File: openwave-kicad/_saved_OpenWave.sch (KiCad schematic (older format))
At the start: 38 parts, among them IC1 STM32F405RGT, J1 USB_OTG, J2 503182-1852, SW1 SW_Push, Y1 8MHz, Y2 32.768KHz

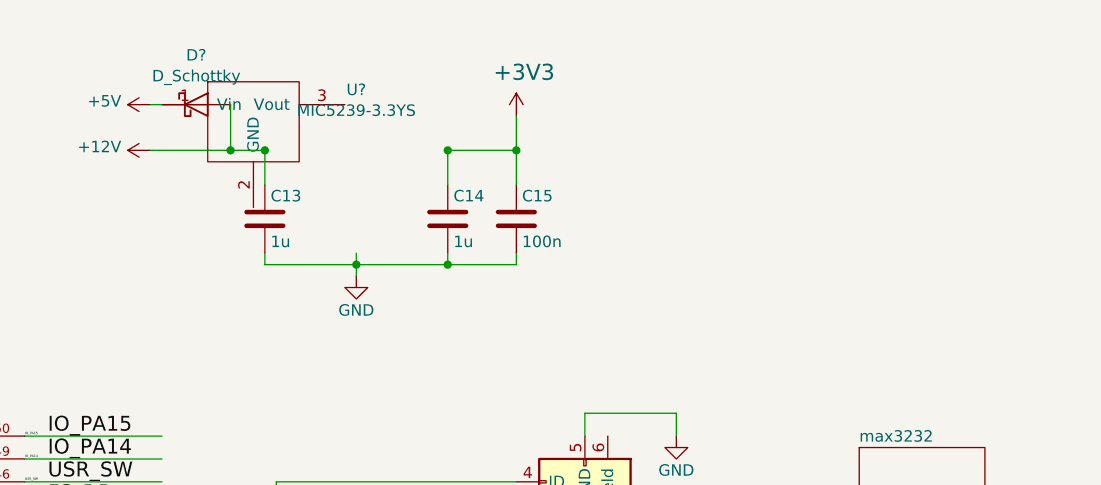
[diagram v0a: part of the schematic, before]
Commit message: added bluetooth header, 4.2v reg
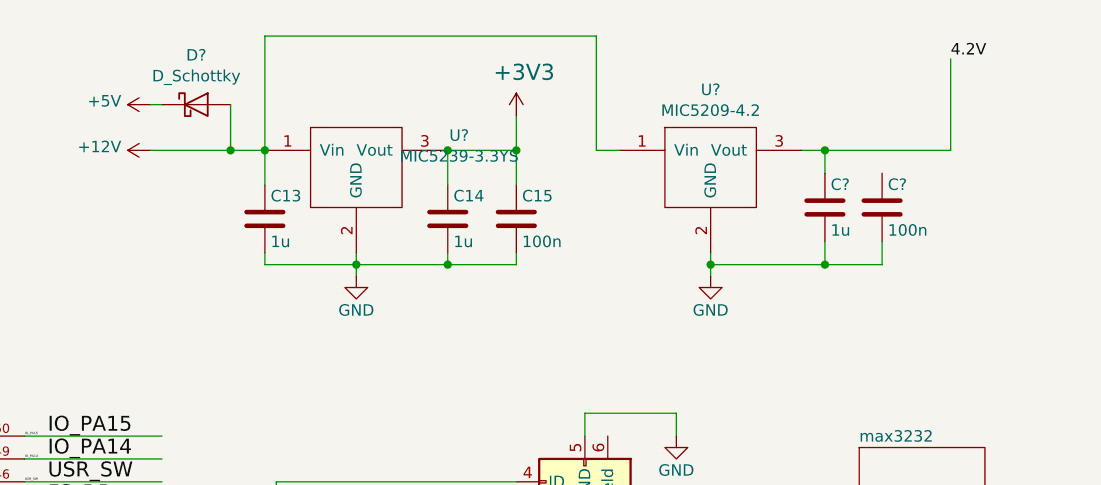
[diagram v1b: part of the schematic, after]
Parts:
- added C?: 1u, Capacitors_SMD:C_0603, symbol Device:C
- added C?: 100n, Capacitors_SMD:C_0603, symbol Device:C
- added U?: MIC5209-4.2, symbol wattnotions:MIC5209-4.2
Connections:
- net labels added: 4.2V
- wire segments 188 -> 202
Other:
- moved on the sheet: U?
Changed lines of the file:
@@
 L wattnotions:MIC5239-3.3YS U?
 U 1 1 5CAAC9EC
-P 8150 1000
-F 0 "U?" H 8150 1165 50  0000 C CNN
-F 1 "MIC5239-3.3YS" H 8150 1074 50  0000 C CNN
-F 2 "" H 8150 950 50  0001 C CNN
-F 3 "" H 8150 950 50  0001 C CNN
-	1    8150 1000
+P 8600 1200
+F 0 "U?" H 8600 1365 50  0000 C CNN
+F 1 "MIC5239-3.3YS" H 8600 1274 50  0000 C CNN
+F 2 "" H 8600 1150 50  0001 C CNN
+F 3 "" H 8600 1150 50  0001 C CNN
+	1    8600 1200
 	1    0    0    -1
 $EndComp
@@
 Wire Wire Line
 	7250 1100 7600 1100
+$Comp
+L wattnotions:MIC5209-4.2 U?
+U 1 1 5CB69853
+P 9700 1150
+F 0 "U?" H 9700 1465 50  0000 C CNN
+F 1 "MIC5209-4.2" H 9700 1374 50  0000 C CNN
+F 2 "" H 9700 1150 50  0001 C CNN
+F 3 "" H 9700 1150 50  0001 C CNN
+	1    9700 1150
+	1    0    0    -1
+$EndComp
+Wire Wire Line
+	7750 1100 7750 600
+Wire Wire Line
+	7750 600  9200 600
+Wire Wire Line
+	9200 600  9200 1100
+Wire Wire Line
+	9200 1100 9300 1100
+$Comp
+L power:GND #PWR?
+U 1 1 5CB73D5D
+P 9700 1650
+F 0 "#PWR?" H 9700 1400 50  0001 C CNN
+F 1 "GND" H 9700 1500 50  0000 C CNN
+F 2 "" H 9700 1650 50  0001 C CNN
+F 3 "" H 9700 1650 50  0001 C CNN
+	1    9700 1650
+	1    0    0    -1
+$EndComp
+Wire Wire Line
+	9700 1550 9700 1600
+$Comp
+L Device:C C?
+U 1 1 5CB7E204
+P 10200 1350
+F 0 "C?" H 10225 1450 50  0000 L CNN
+F 1 "1u" H 10225 1250 50  0000 L CNN
+F 2 "Capacitors_SMD:C_0603" H 10238 1200 50  0001 C CNN
+F 3 "" H 10200 1350 50  0001 C CNN
+	1    10200 1350
+	1    0    0    -1
+$EndComp
+$Comp
+L Device:C C?
+U 1 1 5CB7E28A
+P 10450 1350
+F 0 "C?" H 10475 1450 50  0000 L CNN
+F 1 "100n" H 10475 1250 50  0000 L CNN
+F 2 "Capacitors_SMD:C_0603" H 10488 1200 50  0001 C CNN
+F 3 "" H 10450 1350 50  0001 C CNN
+	1    10450 1350
+	1    0    0    -1
+$EndComp
+Wire Wire Line
+	10100 1100 10200 1100
+Wire Wire Line
+	10200 1100 10200 1200
+Connection ~ 10200 1100
+Wire Wire Line
+	10200 1100 10750 1100
+Wire Wire Line
+	10200 1500 10200 1600
+Wire Wire Line
+	10200 1600 9700 1600
+Connection ~ 9700 1600
+Wire Wire Line
+	9700 1600 9700 1650
+Wire Wire Line
+	10450 1500 10450 1600
+Wire Wire Line
+	10450 1600 10200 1600
+Connection ~ 10200 1600
+Text Label 10750 700  0    50   ~ 0
+4.2V
+Wire Wire Line
+	10750 700  10750 1100
 $EndSCHEMATC

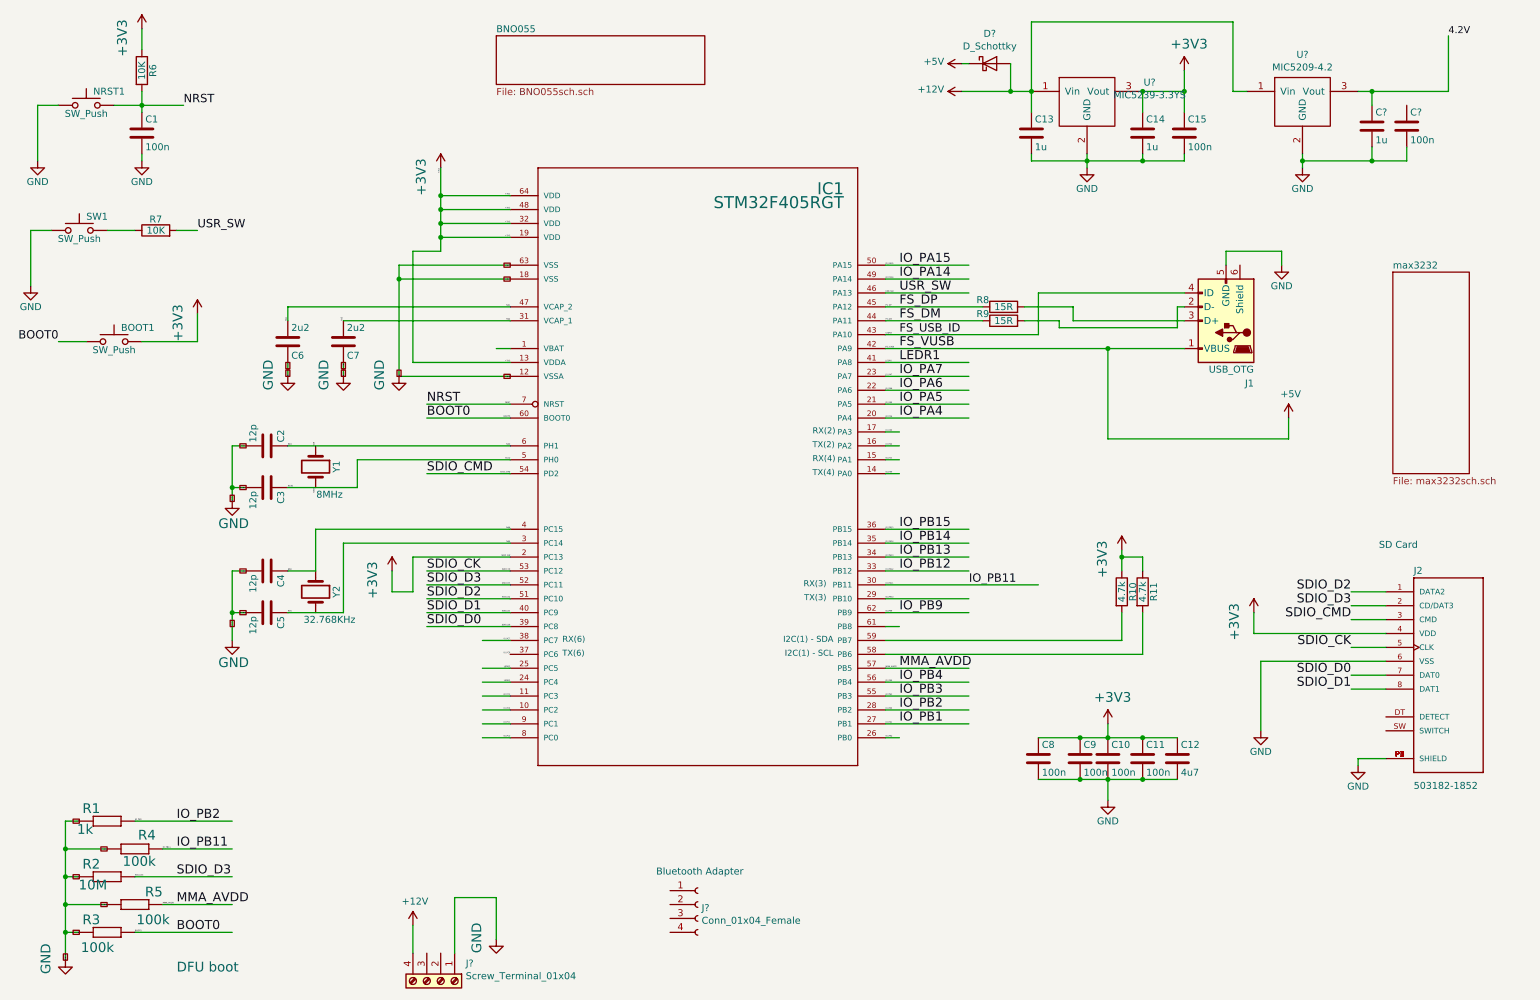
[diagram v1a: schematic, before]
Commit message: linked all footprints to symbols, ready for routing
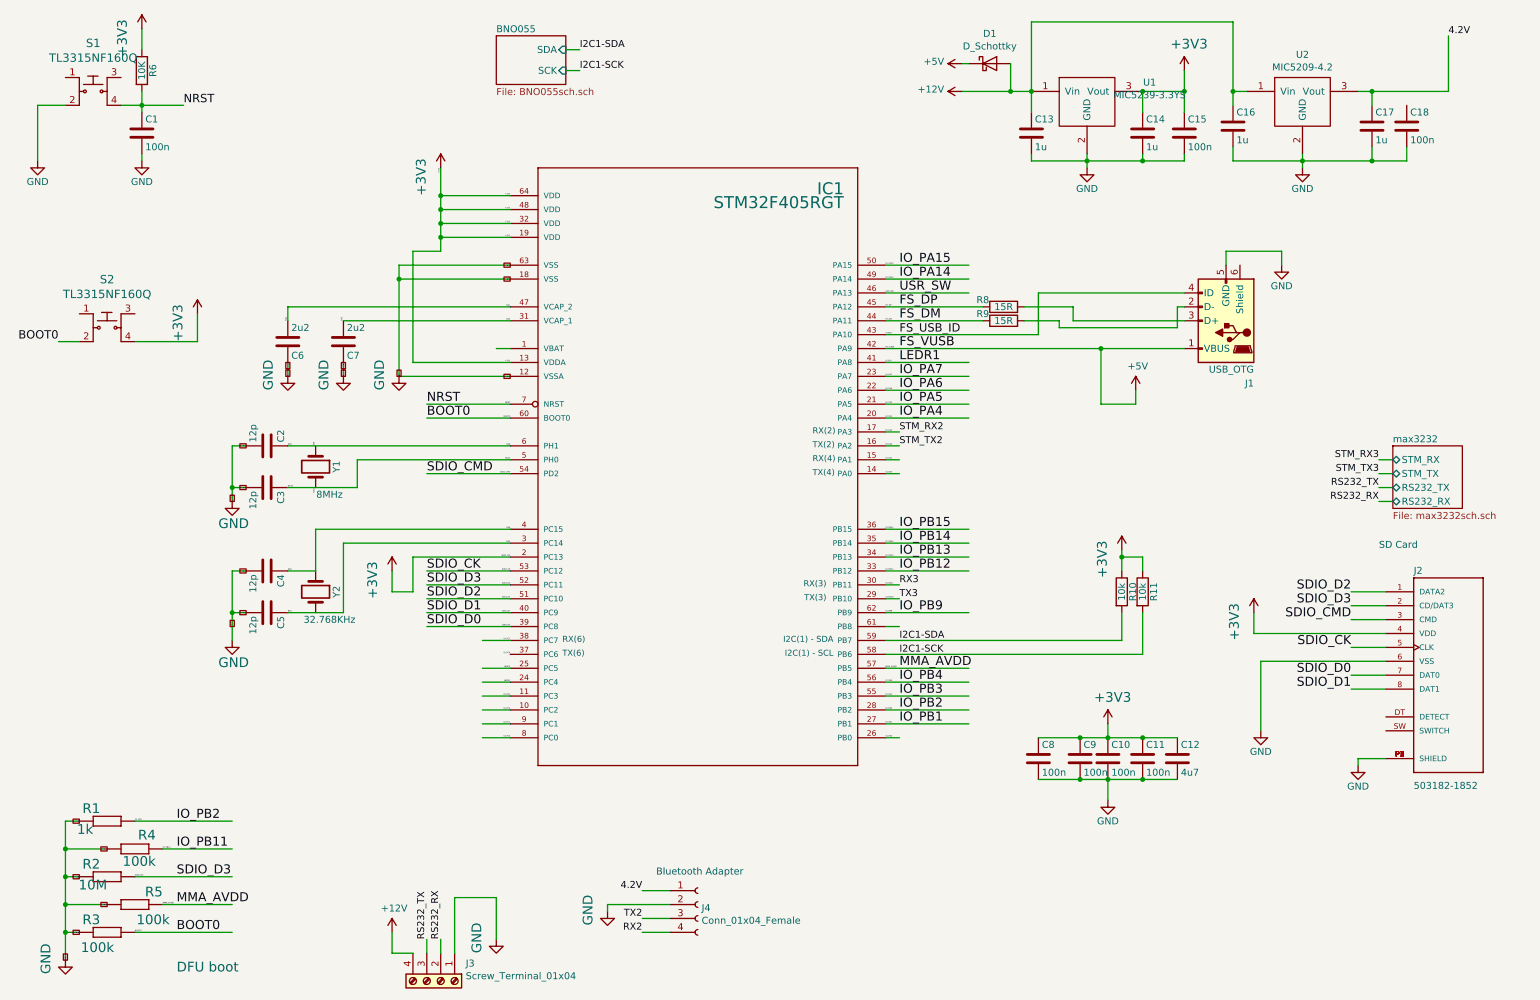
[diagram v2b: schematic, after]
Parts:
- removed BOOT1, NRST1, SW1: SW_Push, symbol Switch:SW_Push
- removed R7: 10K, Resistors_SMD:R_0603, symbol Device:R
- added C16: 1u, Capacitor_SMD:C_0603_1608Metric, symbol Device:C
- added S1, S2: TL3315NF160Q, digikey-footprints:Switch_Tactile_SMD_4.5x4.5mm_TL3315NF160Q, symbol dk_Tactile-Switches:TL3315NF160Q
- C1, C10, C11, C12, C13, C14, C15, C2, C3, C4, C5, C6, C7, C8, C9: footprint Capacitors_SMD:C_0603 -> Capacitor_SMD:C_0603_1608Metric
- C17, C18: renamed from C?; footprint Capacitors_SMD:C_0603 -> Capacitor_SMD:C_0603_1608Metric
- D1: renamed from D?; footprint (none) -> Diode_SMD:D_0201_0603Metric
- J1: footprint (none) -> my_footprints:USB_Micro-B_Molex-105017-0001
- J3: renamed from J?; footprint (none) -> my_footprints:4-WAY-PCB_SOCKET
- J4: renamed from J?; footprint (none) -> Connector_PinHeader_2.54mm:PinHeader_1x04_P2.54mm_Vertical
- R1, R2, R3, R4, R5, R6, R8, R9: footprint Resistors_SMD:R_0603 -> Resistor_SMD:R_0603_1608Metric
- R10, R11: value 4.7k -> 10k; footprint Resistors_SMD:R_0603 -> Resistor_SMD:R_0603_1608Metric
- U1, U2: renamed from U?; footprint (none) -> Package_TO_SOT_SMD:SOT-223-3_TabPin2
- Y1: footprint minibuoy:QC5CA8_8mhz_oscillator -> my_footprints:QC5CA8_8mhz_oscillator
- Y2: footprint minibuoy:ABS06-32.768KHZ_smd_crystal -> my_footprints:ABS06-32.768KHZ_smd_crystal
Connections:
- net labels added: I2C1-SCK, I2C1-SDA, RS232_RX, RS232_TX, RX2, RX3, STM_RX2, STM_RX3, STM_TX2, STM_TX3, TX2, TX3
- wire segments 202 -> 215
